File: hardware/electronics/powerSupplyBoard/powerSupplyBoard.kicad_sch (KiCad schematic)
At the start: 27 parts, among them J1 USB_C_Receptacle_USB2.0, J3 615004143821, J4 PRPC009SBAN-M71RC, SW1 PTS647, SW2 SS-12D07, U1 STM32L052K6, U2 AP2112K-3.3, U3 SN65HVD230QDR, Y1 ECS-327ATQMV

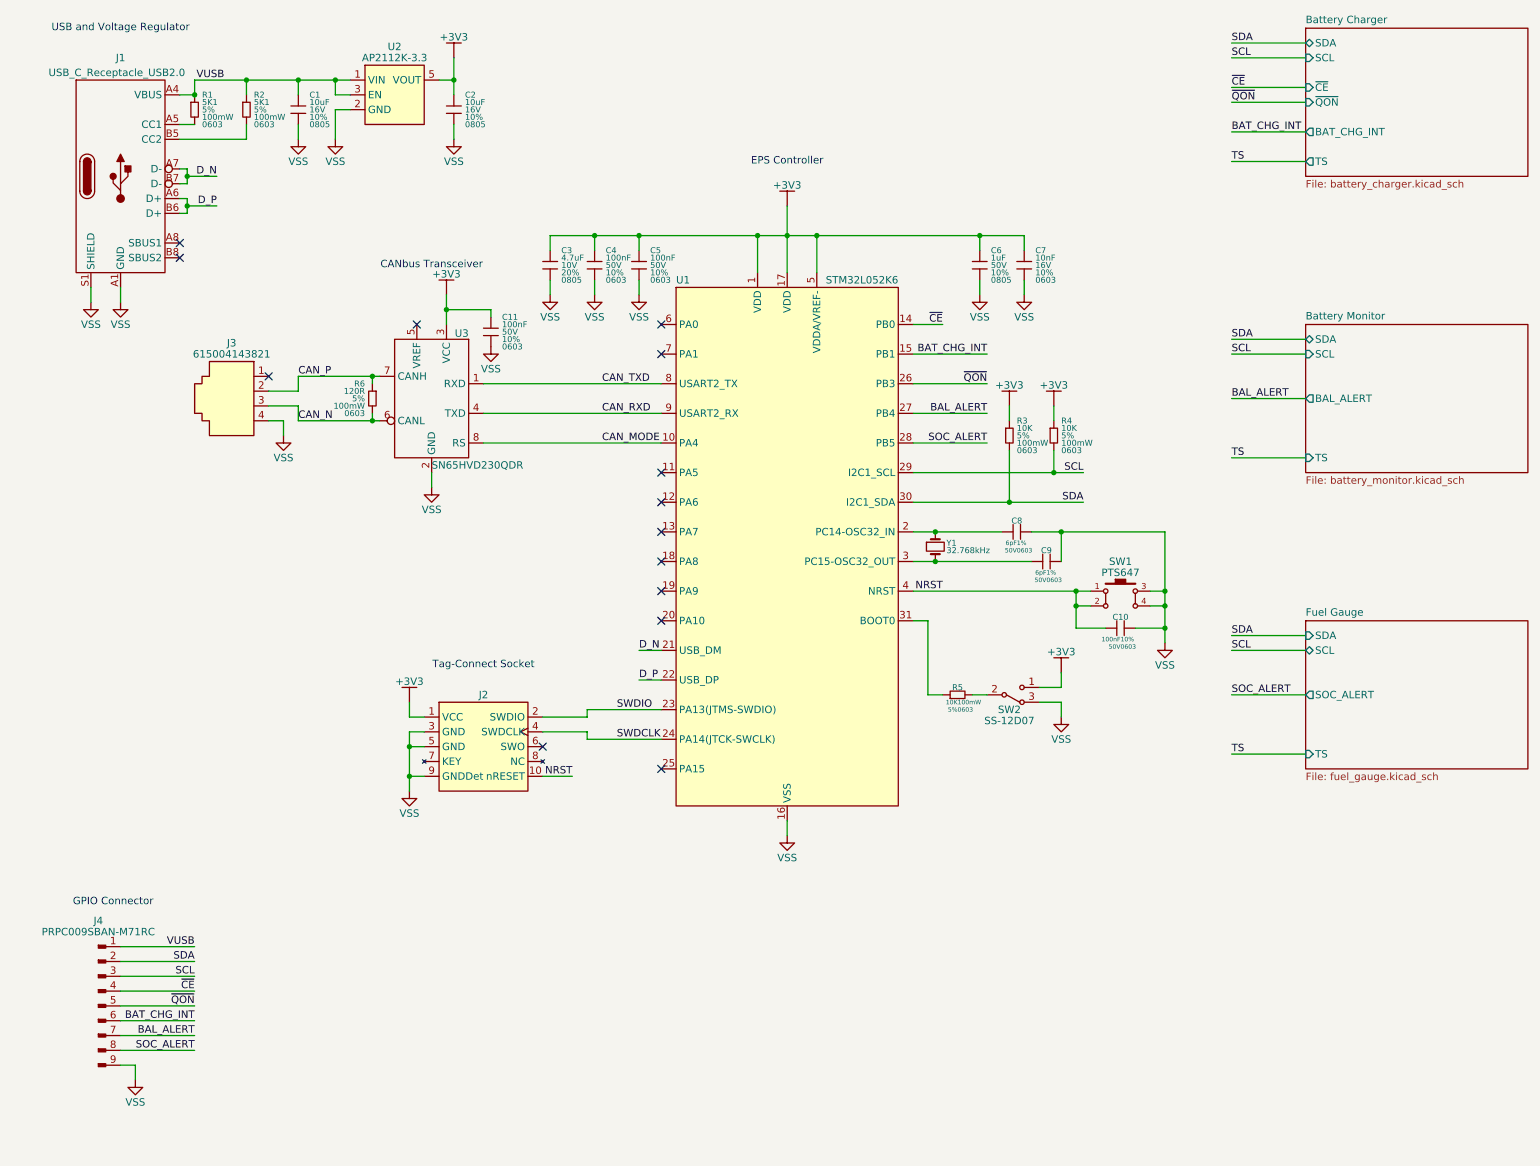
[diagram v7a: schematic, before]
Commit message: added block titles and renamed sheet
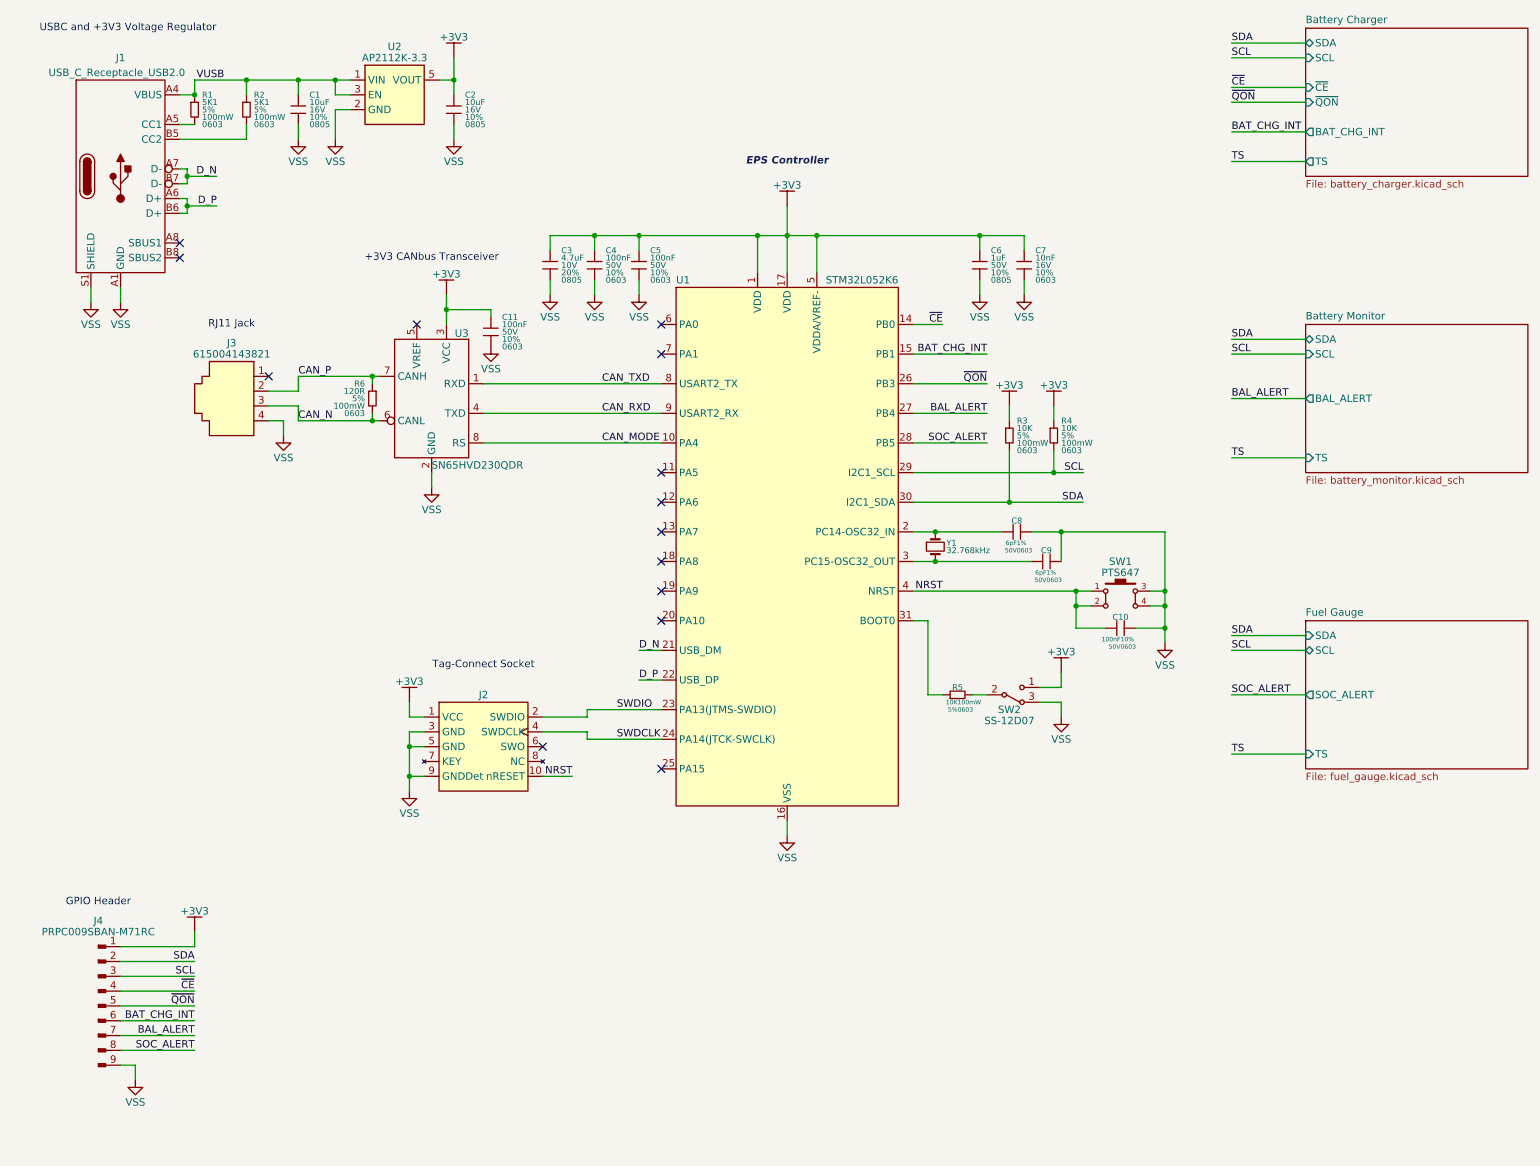
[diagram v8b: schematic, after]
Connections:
- net +3V3: now also J4.1
- net VUSB: no longer J4.1
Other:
- note added: "+3V3 CANbus Transceiver"
- note added: "GPIO Header"
- note added: "RJ11 Jack"
- note added: "USBC and +3V3 Voltage Regulator"
- note removed: "CANbus Transceiver"
- note removed: "GPIO Connector"
- note removed: "USB and Voltage Regulator"
- title: BMS Breakout Board -> Awohali Power Supply
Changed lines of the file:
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@@
 	(paper "USLetter")
 	(title_block
-		(title "BMS Breakout Board")
-		(date "2024-11-01")
+		(title "Awohali Power Supply")
+		(date "2024-11-03")
 		(rev "01")
 		(comment 2 "PROTOTYPE")
@@
 	(wire
 		(pts
-			(xy 25.4 170.18) (xy 38.1 170.18)
-		)
-		(stroke
-			(width 0)
-			(type default)
-		)
-	)
-	(wire
-		(pts
 			(xy 81.28 58.42) (xy 81.28 60.96)
 		)
@@
 	(wire
 		(pts
+			(xy 38.1 170.18) (xy 25.4 170.18)
+		)
+		(stroke
+			(width 0)
+			(type default)
+		)
+	)
+	(wire
+		(pts
 			(xy 106.68 55.88) (xy 106.68 58.42)
 		)
@@
 	(wire
 		(pts
+			(xy 38.1 167.64) (xy 38.1 170.18)
+		)
+		(stroke
+			(width 0)
+			(type default)
+		)
+	)
+	(wire
+		(pts
 			(xy 204.47 109.22) (xy 201.93 109.22)
 		)
@@
 		)
 	)
+	(text "RJ11 Jack"
+		(exclude_from_sim no)
+		(at 44.45 63.5 0)
+		(effects
+			(font
+				(size 1.27 1.27)
+			)
+		)
+	)
 	(text "EPS Controller"
 		(exclude_from_sim no)
@@
 			(font
 				(size 1.27 1.27)
+				(thickness 0.254)
+				(bold yes)
+				(italic yes)
 			)
 		)
 	)
-	(text "CANbus Transceiver"
+	(text "+3V3 CANbus Transceiver"
 		(exclude_from_sim no)
-		(at 78.74 53.34 0)
+		(at 78.74 52.07 0)
 		(effects
 			(font
@@
 		)
 	)
-	(text "USB and Voltage Regulator"
+	(text "USBC and +3V3 Voltage Regulator"
 		(exclude_from_sim no)
-		(at 25.4 12.7 0)
+		(at 26.67 12.7 0)
 		(effects
 			(font
@@
 		)
 	)
-	(text "GPIO Connector"
+	(text "GPIO Header"
 		(exclude_from_sim no)
-		(at 24.13 162.56 0)
+		(at 21.59 162.56 0)
 		(effects
 			(font
@@
 		)
 	)
-	(label "VUSB"
-		(at 38.1 170.18 180)
-		(fields_autoplaced yes)
-		(effects
-			(font
-				(size 1.27 1.27)
-			)
-			(justify right bottom)
-		)
-	)
 	(label "SCL"
 		(at 215.9 17.78 0)
@@
 					(unit 1)
 				)
+			)
+		)
+	)
+	(symbol
+		(lib_id "lib_sch:+3V3")
+		(at 38.1 167.64 0)
+		(unit 1)
+		(exclude_from_sim no)
+		(in_bom yes)
+		(on_board yes)
+		(dnp no)
+		(fields_autoplaced yes)
+		(property "Reference" "#PWR036"
+			(at 38.1 167.64 0)
+			(effects
+				(font
+					(size 1.27 1.27)
+				)
+				(hide yes)
+			)
+		)
+		(property "Value" "+3V3"
+			(at 38.1 164.084 0)
+			(do_not_autoplace yes)
+			(effects
+				(font
+					(size 1.27 1.27)
+				)
+			)
+		)
+		(property "Footprint" ""
+			(at 38.1 167.64 0)
+			(effects
+				(font
+					(size 1.27 1.27)
+				)
+				(hide yes)
+			)
+		)
+		(property "Datasheet" ""
+			(at 38.1 167.64 0)
+			(effects
+				(font
+					(size 1.27 1.27)
+				)
+				(hide yes)
+			)
+		)
+		(property "Description" ""
+			(at 38.1 167.64 0)
+			(effects
+				(font
+					(size 1.27 1.27)
+				)
+				(hide yes)
+			)
+		)
+		(pin "1"
+		)
+		(instances
+			(project ""
+				(path "/6f3ae1d2-e925-4178-b812-ea14ec542b6c"
+					(reference "#PWR036")
+					(unit 1)
+				)
